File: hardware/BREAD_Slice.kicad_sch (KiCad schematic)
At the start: 0 parts

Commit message: did schematic
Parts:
- added J1: Screw_Terminal_01x02, TerminalBlock:TerminalBlock_MaiXu_MX126-5.0-02P_1x02_P5.00mm, symbol Connector:Screw_Terminal_01x02
- added SW1: SW_SPDT, Button_Switch_THT:SW_Slide-03_Wuerth-WS-SLTV_10x2.5x6.4_P2.54mm, symbol Switch:SW_SPDT
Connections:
- net +12V: now also SW1.1 (A)
- net GND: now also J1.2 (Pin_2)
- new net: J1.1 (Pin_1), SW1.3 (C)
- new net VM: SW1.2 (B)
- no-connect marks 25 -> 3
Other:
- added sheet Stepper_card (Stepper_card.kicad_sch)
- added sheet Stepper_card1 (Stepper_card.kicad_sch)
- added sheet Stepper_card2 (Stepper_card.kicad_sch)
- added sheet Stepper_card3 (Stepper_card.kicad_sch)
- title: (none) -> Slice_STPC

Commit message: more routing
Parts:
- removed SW1: SW_SPDT, Button_Switch_THT:SW_Slide-03_Wuerth-WS-SLTV_10x2.5x6.4_P2.54mm, symbol Switch:SW_SPDT
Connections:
- net VM: now also J1.1 (Pin_1)
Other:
- moved on the sheet: J1
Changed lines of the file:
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@@
 	(wire
 		(pts
-			(xy 157.48 180.34) (xy 157.48 182.88)
+			(xy 82.55 208.28) (xy 82.55 210.82)
 		)
 		(stroke
@@
 	(wire
 		(pts
+			(xy 82.55 203.2) (xy 82.55 205.74)
+		)
+		(stroke
+			(width 0)
+			(type default)
+		)
+	)
+	(wire
+		(pts
 			(xy 45.72 72.39) (xy 52.07 72.39)
 		)
@@
 			(type default)
 			(color 194 0 194 1)
-		)
-	)
-	(wire
-		(pts
-			(xy 157.48 177.8) (xy 176.53 177.8)
-		)
-		(stroke
-			(width 0)
-			(type default)
 		)
 	)
@@
 	(symbol
 		(lib_id "Connector:Screw_Terminal_01x02")
-		(at 152.4 177.8 0)
+		(at 77.47 205.74 0)
 		(mirror y)
 		(unit 1)
@@
 		(on_board yes)
 		(dnp no)
-		(fields_autoplaced yes)
 		(property "Reference" "J1"
-			(at 152.4 171.45 0)
+			(at 77.47 203.454 0)
 			(effects
 				(font
@@
 		)
 		(property "Value" "Screw_Terminal_01x02"
-			(at 152.4 173.99 0)
-			(effects
-				(font
-					(size 1.27 1.27)
-				)
+			(at 77.47 201.93 0)
+			(effects
+				(font
+					(size 1.27 1.27)
+				)
+				(hide yes)
 			)
 		)
 		(property "Footprint" "TerminalBlock:TerminalBlock_MaiXu_MX126-5.0-02P_1x02_P5.00mm"
-			(at 152.4 177.8 0)
+			(at 77.47 205.74 0)
 			(effects
 				(font
@@
 		)
 		(property "Datasheet" "~"
-			(at 152.4 177.8 0)
+			(at 77.47 205.74 0)
 			(effects
 				(font
@@
 		)
 		(property "Description" "Generic screw terminal, single row, 01x02, script generated (kicad-library-utils/schlib/autogen/connector/)"
-			(at 152.4 177.8 0)
+			(at 77.47 205.74 0)
 			(effects
 				(font
@@
 	(symbol
 		(lib_id "power:+12V")
-		(at 176.53 172.72 90)
-		(unit 1)
-		(exclude_from_sim no)
-		(in_bom yes)
-		(on_board yes)
-		(dnp no)
-		(property "Reference" "#PWR013"
-			(at 180.34 172.72 0)
-			(effects
-				(font
-					(size 1.27 1.27)
-				)
-				(hide yes)
-			)
-		)
-		(property "Value" "+12V"
-			(at 172.974 172.72 0)
-			(effects
-				(font
-					(size 1.27 1.27)
-				)
-			)
-		)
-		(property "Footprint" ""
-			(at 176.53 172.72 0)
-			(effects
-				(font
-					(size 1.27 1.27)
-				)
-				(hide yes)
-			)
-		)
-		(property "Datasheet" ""
-			(at 176.53 172.72 0)
-			(effects
-				(font
-					(size 1.27 1.27)
-				)
-				(hide yes)
-			)
-		)
-		(property "Description" "Power symbol creates a global label with name \"+12V\""
-			(at 176.53 172.72 0)
-			(effects
-				(font
-					(size 1.27 1.27)
-				)
-				(hide yes)
-			)
-		)
-		(pin "1"
-		)
-		(instances
-			(project "BREAD_Slice"
-				(path "/66043bca-a260-4915-9fce-8a51d324c687"
-					(reference "#PWR013")
-					(unit 1)
-				)
-			)
-		)
-	)
-	(symbol
-		(lib_id "power:+12V")
 		(at 143.51 105.41 270)
 		(unit 1)
@@
 	(symbol
 		(lib_id "power:+12V")
-		(at 186.69 175.26 270)
+		(at 82.55 203.2 0)
 		(unit 1)
 		(exclude_from_sim no)
@@
 		(dnp no)
 		(property "Reference" "#PWR014"
-			(at 182.88 175.26 0)
+			(at 82.55 207.01 0)
 			(effects
 				(font
@@
 		)
 		(property "Value" "VM"
-			(at 190.246 175.26 0)
+			(at 82.55 199.644 0)
 			(effects
 				(font
@@
 		)
 		(property "Footprint" ""
-			(at 186.69 175.26 0)
+			(at 82.55 203.2 0)
 			(effects
 				(font
@@
 		)
 		(property "Datasheet" ""
-			(at 186.69 175.26 0)
+			(at 82.55 203.2 0)
 			(effects
 				(font
@@
 		)
 		(property "Description" "Power symbol creates a global label with name \"+12V\""
-			(at 186.69 175.26 0)
+			(at 82.55 203.2 0)
 			(effects
 				(font
@@
 	)
 	(symbol
-		(lib_id "Switch:SW_SPDT")
-		(at 181.61 175.26 0)
-		(mirror y)
-		(unit 1)
-		(exclude_from_sim no)
-		(in_bom yes)
-		(on_board yes)
-		(dnp no)
-		(fields_autoplaced yes)
-		(property "Reference" "SW1"
-			(at 181.61 166.37 0)
-			(effects
-				(font
-					(size 1.27 1.27)
-				)
-			)
-		)
-		(property "Value" "SW_SPDT"
-			(at 181.61 168.91 0)
-			(effects
-				(font
-					(size 1.27 1.27)
-				)
-			)
-		)
-		(property "Footprint" "Button_Switch_THT:SW_Slide-03_Wuerth-WS-SLTV_10x2.5x6.4_P2.54mm"
-			(at 181.61 175.26 0)
-			(effects
-				(font
-					(size 1.27 1.27)
-				)
-				(hide yes)
-			)
-		)
-		(property "Datasheet" "~"
-			(at 181.61 182.88 0)
-			(effects
-				(font
-					(size 1.27 1.27)
-				)
-				(hide yes)
-			)
-		)
-		(property "Description" "Switch, single pole double throw"
-			(at 181.61 175.26 0)
-			(effects
-				(font
-					(size 1.27 1.27)
-				)
-				(hide yes)
-			)
-		)
-		(pin "2"
-		)
-		(pin "1"
-		)
-		(pin "3"
-		)
-		(instances
-			(project ""
-				(path "/66043bca-a260-4915-9fce-8a51d324c687"
-					(reference "SW1")
-					(unit 1)
-				)
-			)
-		)
-	)
-	(symbol
 		(lib_id "power:GND")
-		(at 157.48 182.88 0)
+		(at 82.55 210.82 0)
 		(unit 1)
 		(exclude_from_sim no)
@@
 		(dnp no)
 		(property "Reference" "#PWR011"
-			(at 157.48 189.23 0)
+			(at 82.55 217.17 0)
 			(effects
 				(font
@@
 		)
 		(property "Value" "GND"
-			(at 157.48 186.436 0)
+			(at 82.55 214.376 0)
 			(effects
 				(font
@@
 		)
 		(property "Footprint" ""
-			(at 157.48 182.88 0)
+			(at 82.55 210.82 0)
 			(effects
 				(font
@@
 		)
 		(property "Datasheet" ""
-			(at 157.48 182.88 0)
+			(at 82.55 210.82 0)
 			(effects
 				(font
@@
 		)
 		(property "Description" "Power symbol creates a global label with name \"GND\" , ground"
-			(at 157.48 182.88 0)
-			(effects
-				(font
+			(at 82.55 210.82 0)
+			(effects
+				(font

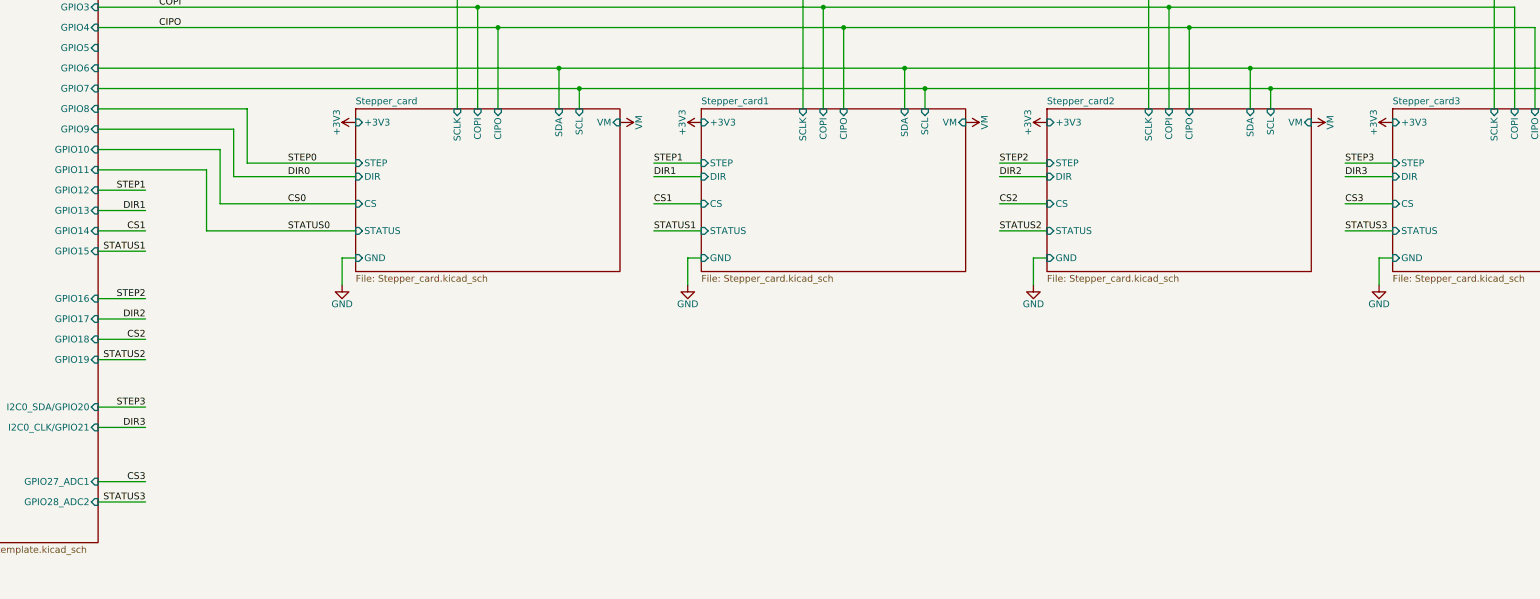
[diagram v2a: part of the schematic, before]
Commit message: finished initial routing
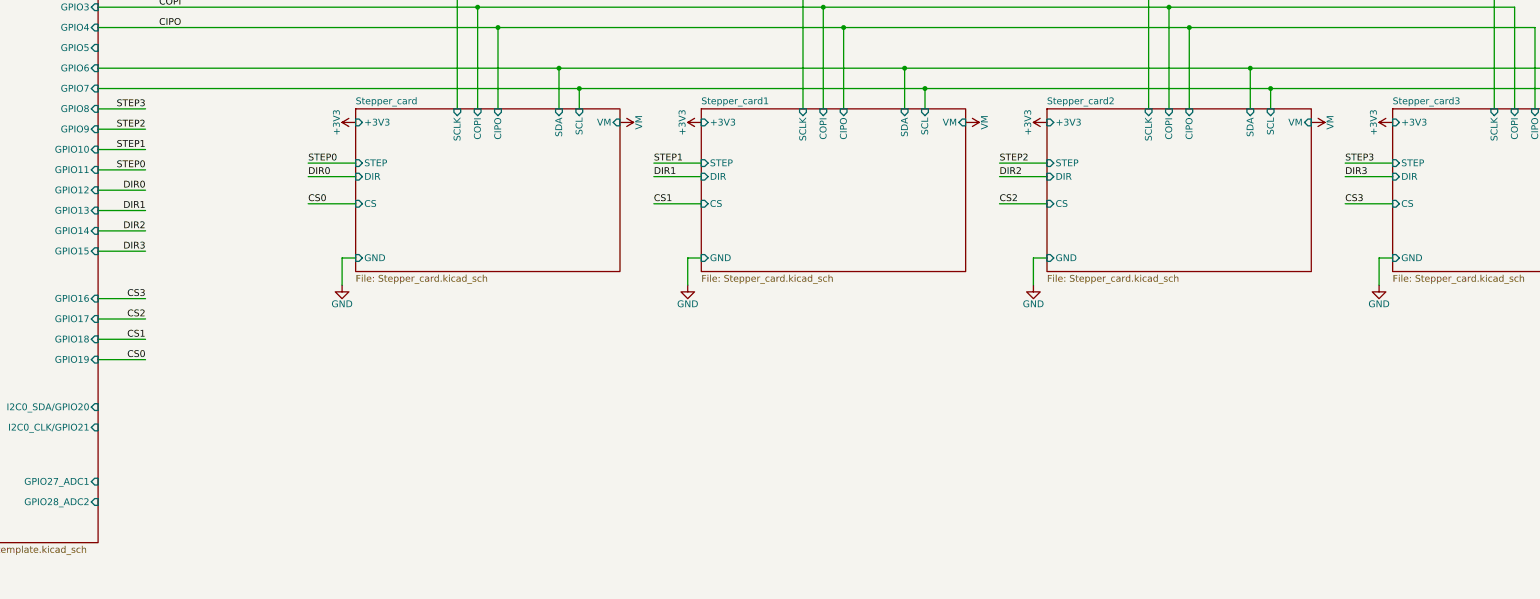
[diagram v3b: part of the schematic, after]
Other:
- sheet Stepper_card ports: added none; removed STATUS
- sheet Stepper_card1 ports: added none; removed STATUS
- sheet Stepper_card2 ports: added none; removed STATUS
- sheet Stepper_card3 ports: added none; removed STATUS

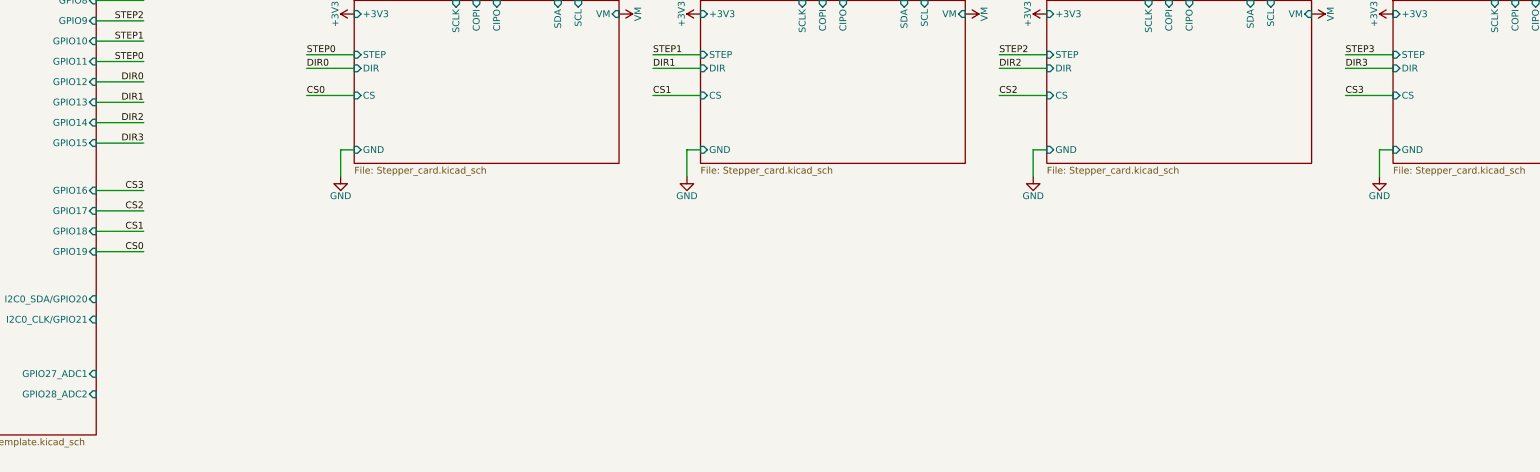
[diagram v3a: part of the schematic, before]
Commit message: added nFAULT line
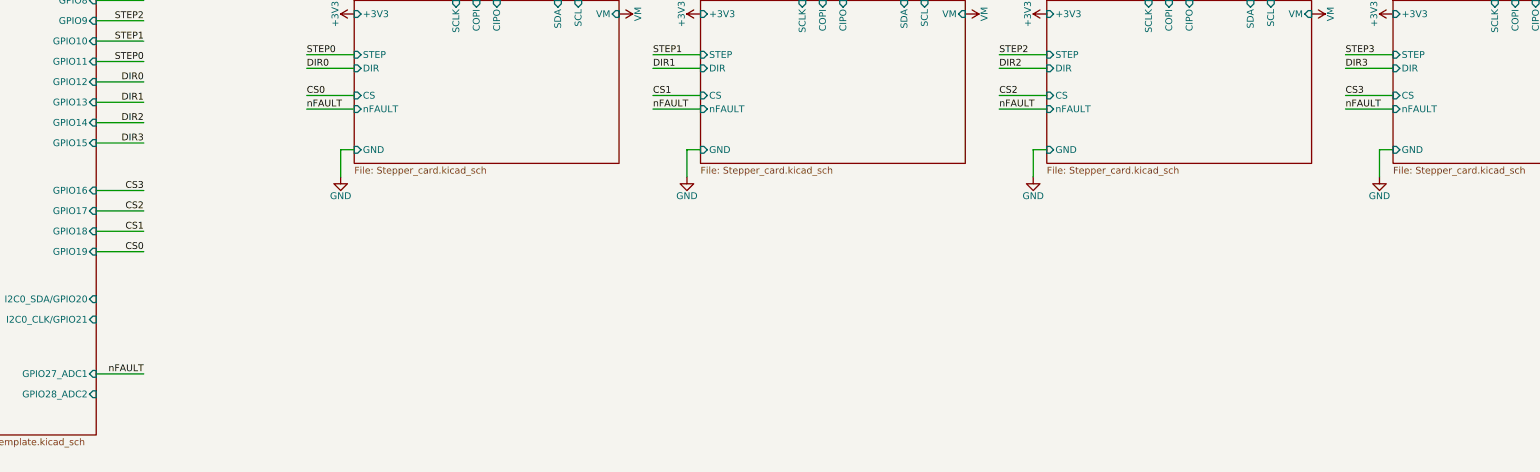
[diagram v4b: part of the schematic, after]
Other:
- sheet Stepper_card ports: added nFAULT; removed none
- sheet Stepper_card1 ports: added nFAULT; removed none
- sheet Stepper_card2 ports: added nFAULT; removed none
- sheet Stepper_card3 ports: added nFAULT; removed none
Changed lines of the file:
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@@
 	(wire
 		(pts
+			(xy 45.72 172.72) (xy 54.61 172.72)
+		)
+		(stroke
+			(width 0.2032)
+			(type default)
+		)
+	)
+	(wire
+		(pts
 			(xy 113.03 80.01) (xy 113.03 102.87)
 		)
@@
 	(wire
 		(pts
+			(xy 158.75 123.19) (xy 149.86 123.19)
+		)
+		(stroke
+			(width 0.2032)
+			(type default)
+		)
+	)
+	(wire
+		(pts
 			(xy 49.53 64.77) (xy 45.72 64.77)
 		)
@@
 	(wire
 		(pts
+			(xy 93.98 123.19) (xy 85.09 123.19)
+		)
+		(stroke
+			(width 0.2032)
+			(type default)
+		)
+	)
+	(wire
+		(pts
 			(xy 196.85 95.25) (xy 196.85 102.87)
 		)
@@
 	(wire
 		(pts
+			(xy 223.52 123.19) (xy 214.63 123.19)
+		)
+		(stroke
+			(width 0.2032)
+			(type default)
+		)
+	)
+	(wire
+		(pts
 			(xy 311.15 83.82) (xy 311.15 102.87)
 		)
@@
 	(wire
 		(pts
+			(xy 288.29 123.19) (xy 279.4 123.19)
+		)
+		(stroke
+			(width 0.2032)
+			(type default)
+		)
+	)
+	(wire
+		(pts
 			(xy 246.38 83.82) (xy 246.38 102.87)
 		)
@@
 		)
 	)
+	(label "nFAULT"
+		(at 214.63 123.19 0)
+		(effects
+			(font
+				(size 1.27 1.27)
+			)
+			(justify left bottom)
+		)
+	)
 	(label "DIR3"
 		(at 54.61 129.54 180)
@@
 		)
 	)
+	(label "nFAULT"
+		(at 54.61 172.72 180)
+		(effects
+			(font
+				(size 1.27 1.27)
+			)
+			(justify right bottom)
+		)
+	)
 	(label "DIR3"
 		(at 279.4 115.57 0)
@@
 		)
 	)
+	(label "nFAULT"
+		(at 279.4 123.19 0)
+		(effects
+			(font
+				(size 1.27 1.27)
+			)
+			(justify left bottom)
+		)
+	)
 	(label "COPI"
 		(at 57.15 83.82 0)
@@
 		)
 	)
+	(label "nFAULT"
+		(at 149.86 123.19 0)
+		(effects
+			(font
+				(size 1.27 1.27)
+			)
+			(justify left bottom)
+		)
+	)
 	(label "STEP2"
 		(at 214.63 113.03 0)
@@
 		)
 	)
+	(label "nFAULT"
+		(at 85.09 123.19 0)
+		(effects
+			(font
+				(size 1.27 1.27)
+			)
+			(justify left bottom)
+		)
+	)
 	(label "DIR1"
 		(at 54.61 121.92 180)
@@
 			)
 		)
+		(pin "nFAULT" input
+			(at 288.29 123.19 180)
+			(effects
+				(font
+					(size 1.27 1.27)
+				)
+				(justify left)
+			)
+		)
 		(instances
 			(project "BREAD_Slice"
@@
 			)
 		)
+		(pin "nFAULT" input
+			(at 93.98 123.19 180)
+			(effects
+				(font
+					(size 1.27 1.27)
+				)
+				(justify left)
+			)
+		)
 		(instances
 			(project "BREAD_Slice"
@@
 			)
 		)
+		(pin "nFAULT" input
+			(at 158.75 123.19 180)
+			(effects
+				(font
+					(size 1.27 1.27)
+				)
+				(justify left)
+			)
+		)
 		(instances
 			(project "BREAD_Slice"
@@
 			(effects
 				(font
+					(size 1.27 1.27)
+				)
+				(justify left)
+			)
+		)
+		(pin "nFAULT" input
+			(at 223.52 123.19 180)
+			(effects
+				(font
